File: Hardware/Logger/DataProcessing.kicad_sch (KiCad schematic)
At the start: 4 parts, among them CN1 Conn_02x19_Odd_Even, CN10 Conn_02x19_Odd_Even, CN2 Conn_02x19_Odd_Even, CN7 Conn_02x19_Odd_Even

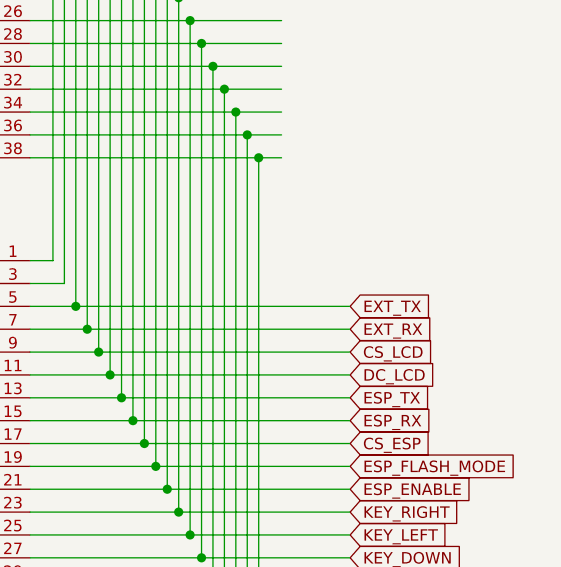
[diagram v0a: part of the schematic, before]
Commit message: 1) LCD works ok now 2) fix #49 3) fix #50
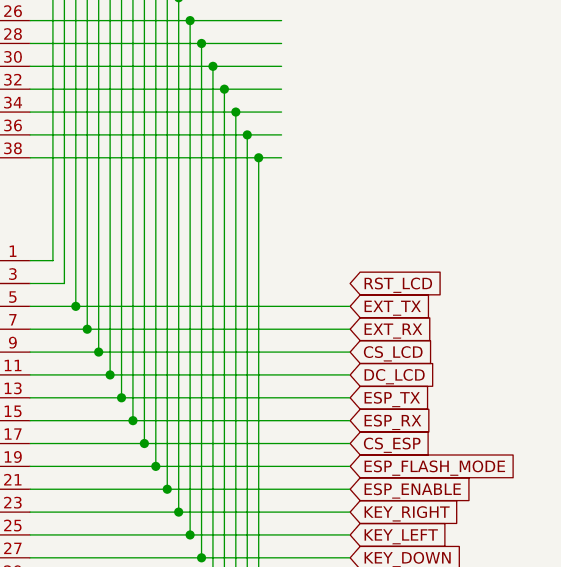
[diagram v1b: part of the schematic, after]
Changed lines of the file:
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@@
+    )
+  )
+  (global_label "RST_LCD" (shape input) (at 238.76 107.95 0) (fields_autoplaced)
+    (effects (font (size 1.27 1.27)) (justify left))
+    (property "Intersheet References" "${INTERSHEET_REFS}" (id 0) (at 249.156 108.0294 0)
+      (effects (font (size 1.27 1.27)) (justify left) hide)
     )
   )

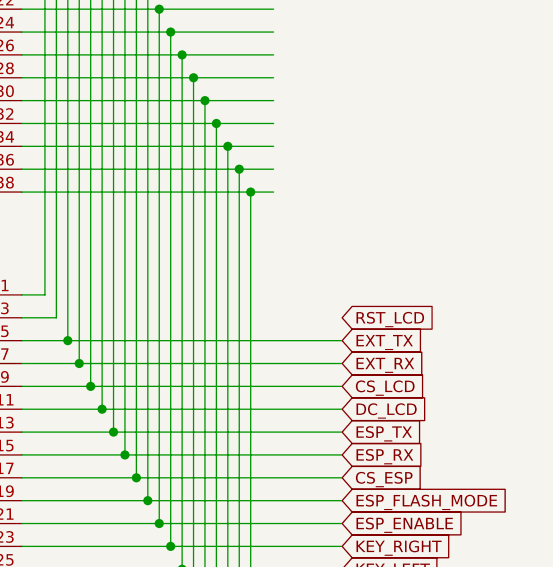
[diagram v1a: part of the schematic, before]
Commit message: fixed SPI connections to SD card, added ESD protection for SD card
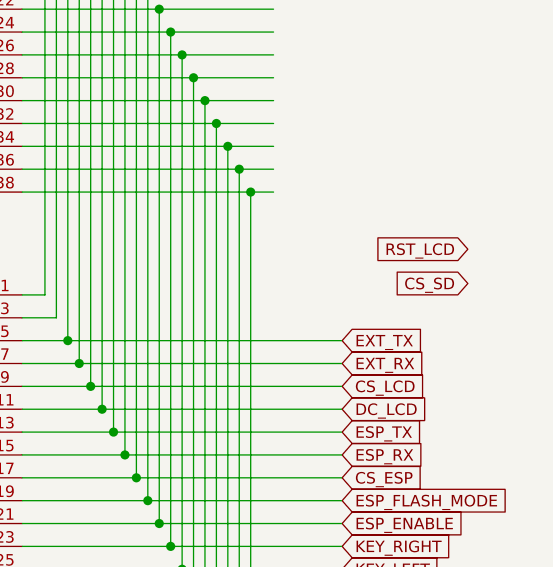
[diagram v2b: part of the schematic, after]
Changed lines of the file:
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@@
-    )
-  )
-  (global_label "RST_LCD" (shape input) (at 238.76 107.95 0) (fields_autoplaced)
-    (effects (font (size 1.27 1.27)) (justify left))
-    (property "Intersheet References" "${INTERSHEET_REFS}" (id 0) (at 249.156 108.0294 0)
-      (effects (font (size 1.27 1.27)) (justify left) hide)
     )
   )
@@
     )
   )
+  (global_label "RST_LCD" (shape input) (at 252.73 100.33 180) (fields_autoplaced)
+    (effects (font (size 1.27 1.27)) (justify right))
+    (property "Intersheet References" "${INTERSHEET_REFS}" (id 0) (at 242.334 100.2506 0)
+      (effects (font (size 1.27 1.27)) (justify right) hide)
+    )
+  )
+  (global_label "CS_SD" (shape input) (at 252.73 104.14 180) (fields_autoplaced)
+    (effects (font (size 1.27 1.27)) (justify right))
+    (property "Intersheet References" "${INTERSHEET_REFS}" (id 0) (at 158.75 -6.35 0)
+      (effects (font (size 1.27 1.27)) hide)
+    )
+  )

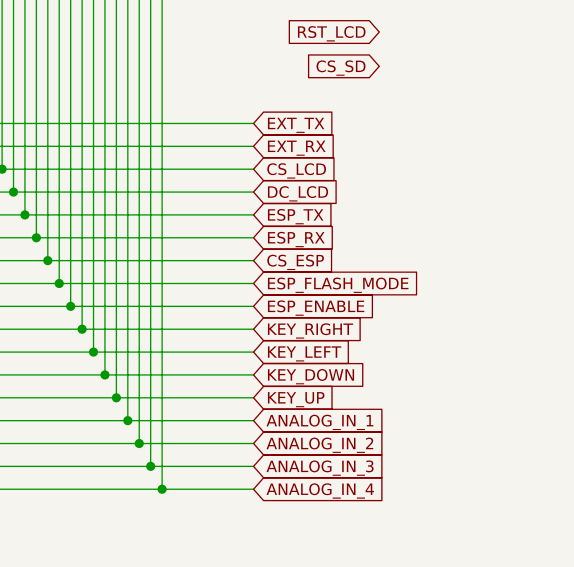
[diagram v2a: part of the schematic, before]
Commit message: PoC of esp32 support (setting esp32 to flashing mode))
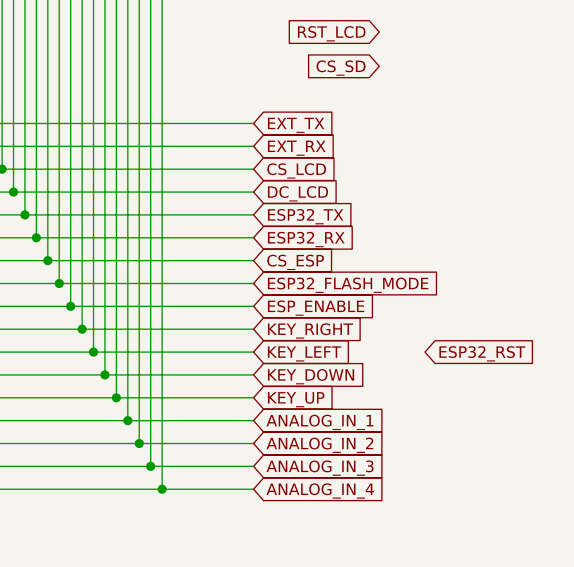
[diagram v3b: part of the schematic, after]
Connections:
- net ESP_FLASH_MODE renamed ESP32_FLASH_MODE
- net ESP_RX renamed ESP32_RX
- net ESP_TX renamed ESP32_TX
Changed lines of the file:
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@@
     )
   )
-  (global_label "ESP_TX" (shape input) (at 238.76 120.65 0) (fields_autoplaced)
+  (global_label "ESP32_TX" (shape input) (at 238.76 120.65 0) (fields_autoplaced)
     (effects (font (size 1.27 1.27)) (justify left))
-    (property "Intersheet References" "${INTERSHEET_REFS}" (id 0) (at -5.08 35.56 0)
-      (effects (font (size 1.27 1.27)) hide)
+    (property "Intersheet References" "${INTERSHEET_REFS}" (id 0) (at 250.3655 120.5706 0)
+      (effects (font (size 1.27 1.27)) (justify left) hide)
     )
   )
-  (global_label "ESP_RX" (shape input) (at 238.76 123.19 0) (fields_autoplaced)
+  (global_label "ESP32_RX" (shape input) (at 238.76 123.19 0) (fields_autoplaced)
     (effects (font (size 1.27 1.27)) (justify left))
-    (property "Intersheet References" "${INTERSHEET_REFS}" (id 0) (at -5.08 35.56 0)
-      (effects (font (size 1.27 1.27)) hide)
+    (property "Intersheet References" "${INTERSHEET_REFS}" (id 0) (at 250.6679 123.1106 0)
+      (effects (font (size 1.27 1.27)) (justify left) hide)
     )
   )
@@
     )
   )
-  (global_label "ESP_FLASH_MODE" (shape input) (at 238.76 128.27 0) (fields_autoplaced)
+  (global_label "ESP32_FLASH_MODE" (shape input) (at 238.76 128.27 0) (fields_autoplaced)
     (effects (font (size 1.27 1.27)) (justify left))
-    (property "Intersheet References" "${INTERSHEET_REFS}" (id 0) (at -1.27 27.94 0)
-      (effects (font (size 1.27 1.27)) hide)
+    (property "Intersheet References" "${INTERSHEET_REFS}" (id 0) (at 260.1021 128.1906 0)
+      (effects (font (size 1.27 1.27)) (justify left) hide)
     )
   )
@@
     )
   )
+  (global_label "ESP32_RST" (shape input) (at 257.81 135.89 0) (fields_autoplaced)
+    (effects (font (size 1.27 1.27)) (justify left))
+    (property "Intersheet References" "${INTERSHEET_REFS}" (id 0) (at 270.6855 135.8106 0)
+      (effects (font (size 1.27 1.27)) (justify left) hide)
+    )
+  )

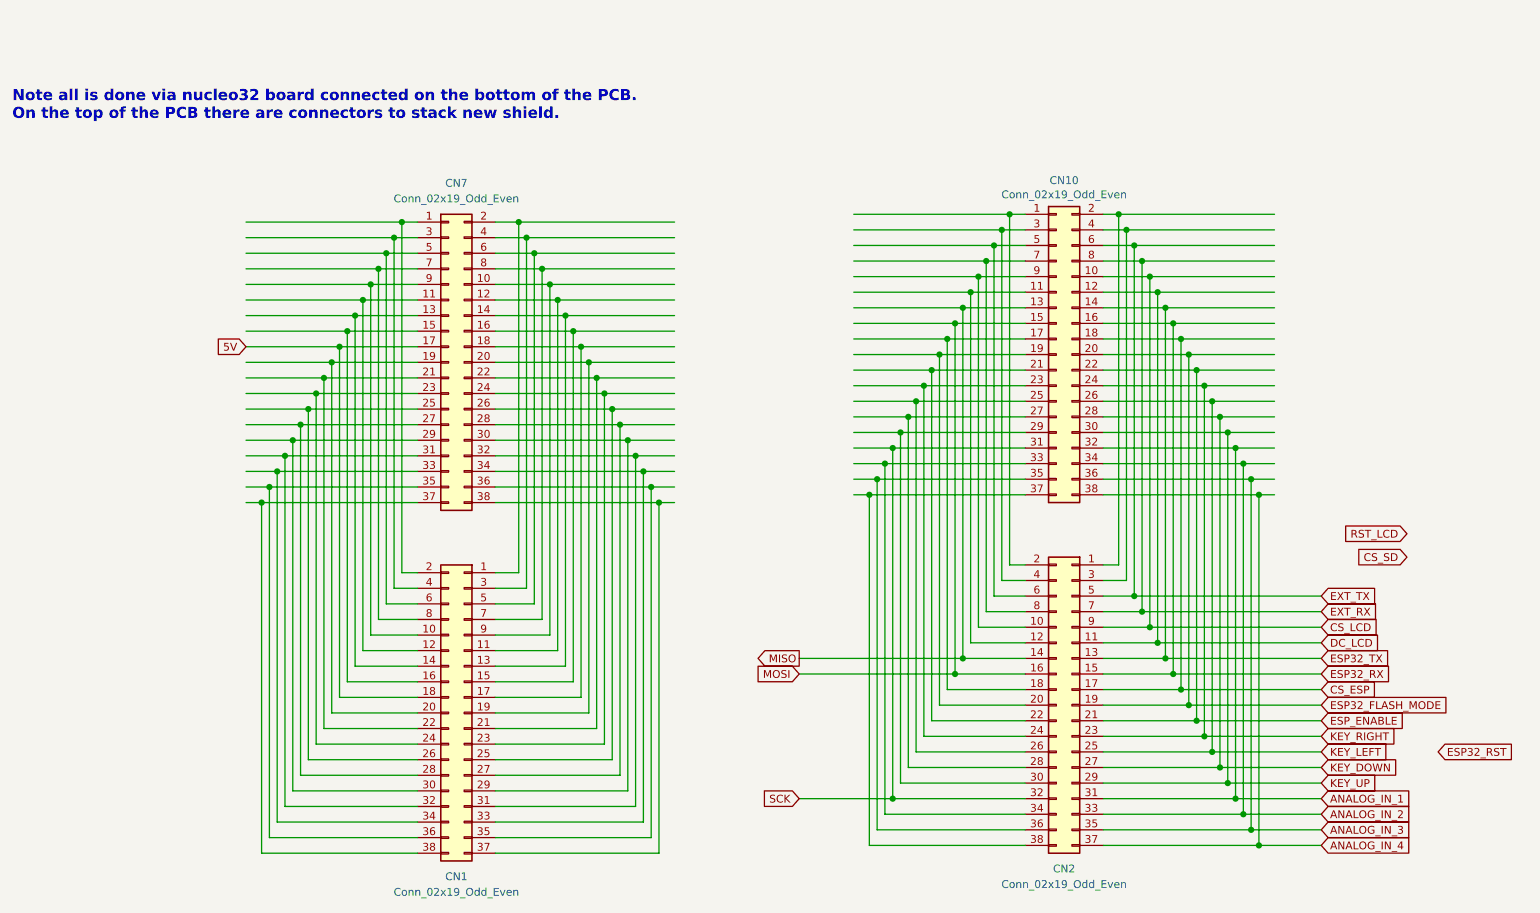
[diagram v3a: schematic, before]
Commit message: apply actual gpio connections to stm32 board, changed photoresistor to phototransistor
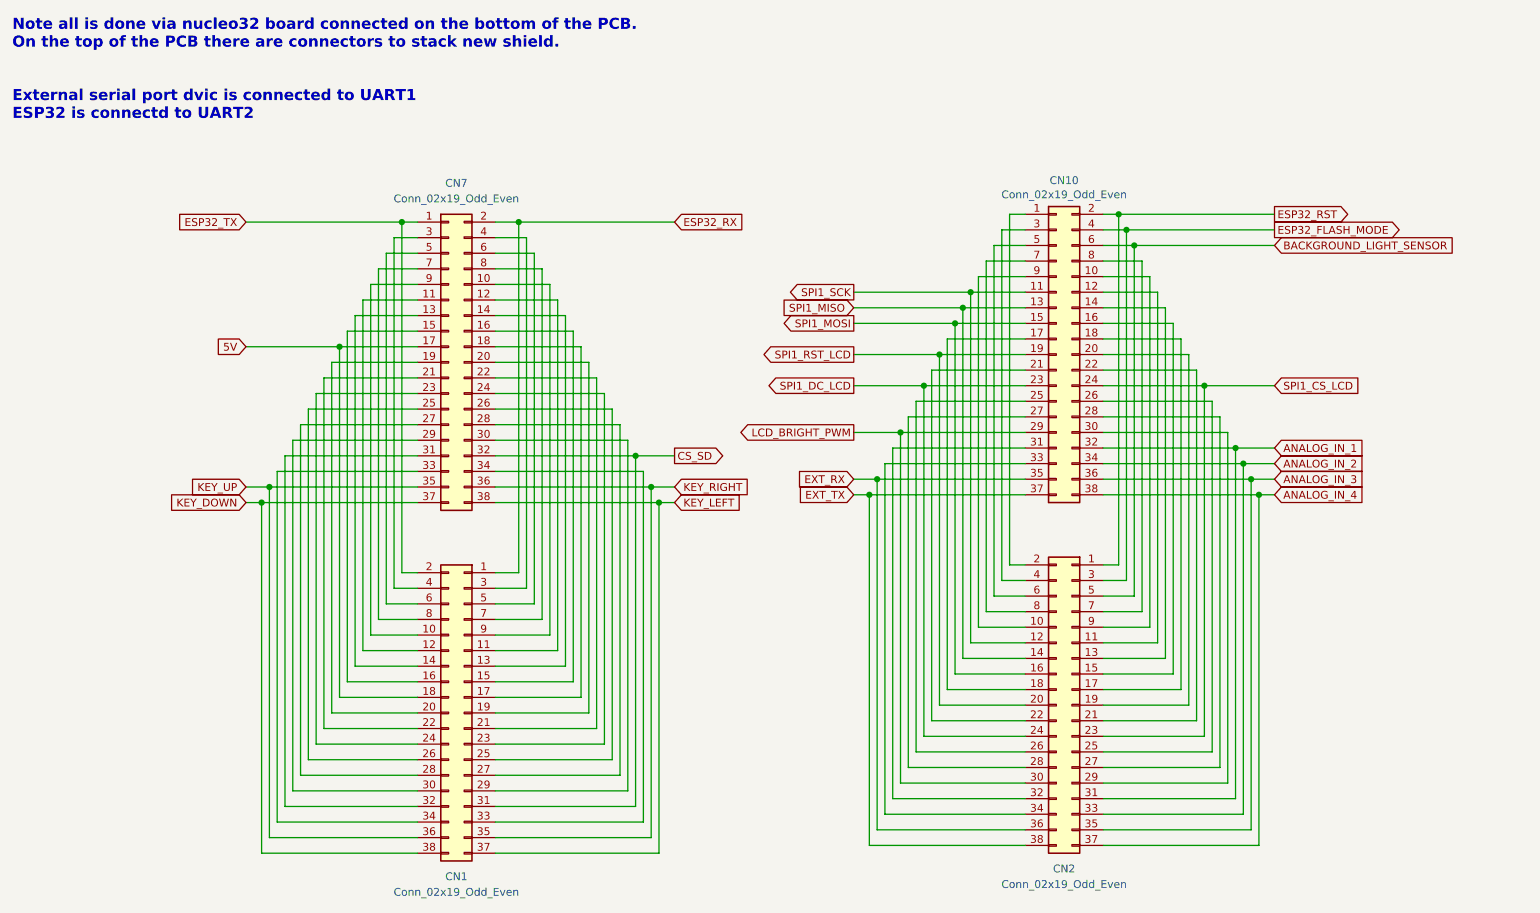
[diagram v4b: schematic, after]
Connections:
- net CS_SD: now also CN1.31 (Pin_31), CN7.32 (Pin_32)
- net ESP32_FLASH_MODE: now also CN10.4 (Pin_4), CN2.3 (Pin_3); no longer CN10.20 (Pin_20), CN2.19 (Pin_19)
- net ESP32_RST: now also CN10.2 (Pin_2), CN2.1 (Pin_1)
- net ESP32_RX: now also CN1.1 (Pin_1), CN7.2 (Pin_2); no longer CN10.16 (Pin_16), CN2.15 (Pin_15)
- net ESP32_TX: now also CN1.2 (Pin_2), CN7.1 (Pin_1); no longer CN10.14 (Pin_14), CN2.13 (Pin_13)
- net EXT_RX: now also CN10.35 (Pin_35), CN2.36 (Pin_36); no longer CN10.8 (Pin_8), CN2.7 (Pin_7)
- net EXT_TX: now also CN10.37 (Pin_37), CN2.38 (Pin_38); no longer CN10.6 (Pin_6), CN2.5 (Pin_5)
- net KEY_DOWN: now also CN1.38 (Pin_38), CN7.37 (Pin_37); no longer CN10.28 (Pin_28), CN2.27 (Pin_27)
- net KEY_LEFT: now also CN1.37 (Pin_37), CN7.38 (Pin_38); no longer CN10.26 (Pin_26), CN2.25 (Pin_25)
- net KEY_RIGHT: now also CN1.35 (Pin_35), CN7.36 (Pin_36); no longer CN10.24 (Pin_24), CN2.23 (Pin_23)
- net KEY_UP: now also CN1.36 (Pin_36), CN7.35 (Pin_35); no longer CN10.30 (Pin_30), CN2.29 (Pin_29)
- net SPI1_SCK: now reaches CN10.11 (Pin_11), CN2.12 (Pin_12)
- net SPI1_RST_LCD: now reaches CN10.19 (Pin_19), CN2.20 (Pin_20)
- net SPI1_DC_LCD: now reaches CN10.23 (Pin_23), CN2.24 (Pin_24)
- net LCD_BRIGHT_PWM: now reaches CN10.29 (Pin_29), CN2.30 (Pin_30)
- net CS_ESP: no longer names the net of CN10.18 (Pin_18), CN2.17 (Pin_17)
- net CS_LCD: no longer names the net of CN10.10 (Pin_10), CN2.9 (Pin_9)
- net DC_LCD: no longer names the net of CN10.12 (Pin_12), CN2.11 (Pin_11)
- net ESP_ENABLE: no longer names the net of CN10.22 (Pin_22), CN2.21 (Pin_21)
- net MISO renamed SPI1_MISO
- net MOSI renamed SPI1_MOSI
- net SCK: no longer names the net of CN10.31 (Pin_31), CN2.32 (Pin_32)
- new net: CN10.14 (Pin_14), CN2.13 (Pin_13)
- new net: CN10.16 (Pin_16), CN2.15 (Pin_15)
- new net: CN10.20 (Pin_20), CN2.19 (Pin_19)
- new net: CN10.26 (Pin_26), CN2.25 (Pin_25)
- new net: CN10.28 (Pin_28), CN2.27 (Pin_27)
- new net: CN10.30 (Pin_30), CN2.29 (Pin_29)
- new net: CN10.8 (Pin_8), CN2.7 (Pin_7)
- new net BACKGROUND_LIGHT_SENSOR: CN10.6 (Pin_6), CN2.5 (Pin_5)
- new net SPI1_CS_LCD: CN10.24 (Pin_24), CN2.23 (Pin_23)
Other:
- note added: "Note all is done via nucleo32 board connected on the bottom of the PCB. On the top of the PCB there are connectors to stack new shield. External serial port dvic is connected to UART1 ESP32 is connectd to UART2"
- note removed: "Note all is done via nucleo32 board connected on the bottom of the PCB. On the top of the PCB there are connectors to stack new shield."
